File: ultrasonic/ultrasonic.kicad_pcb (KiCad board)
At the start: 2 copper layers, 61 x 36.9 mm, 4 parts, among them J1 Conn_01x23_Female, J2 Conn_01x23_Female, J3 Conn_01x07_Female, J5 Conn_01x04_Male

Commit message: new release
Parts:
- J2: footprint Connector_PinHeader_2.54mm:PinHeader_1x23_P2.54mm_Vertical_SMD_Pin1Left -> Connector_PinSocket_2.54mm:PinSocket_1x23_P2.54mm_Vertical_SMD_Pin1Left

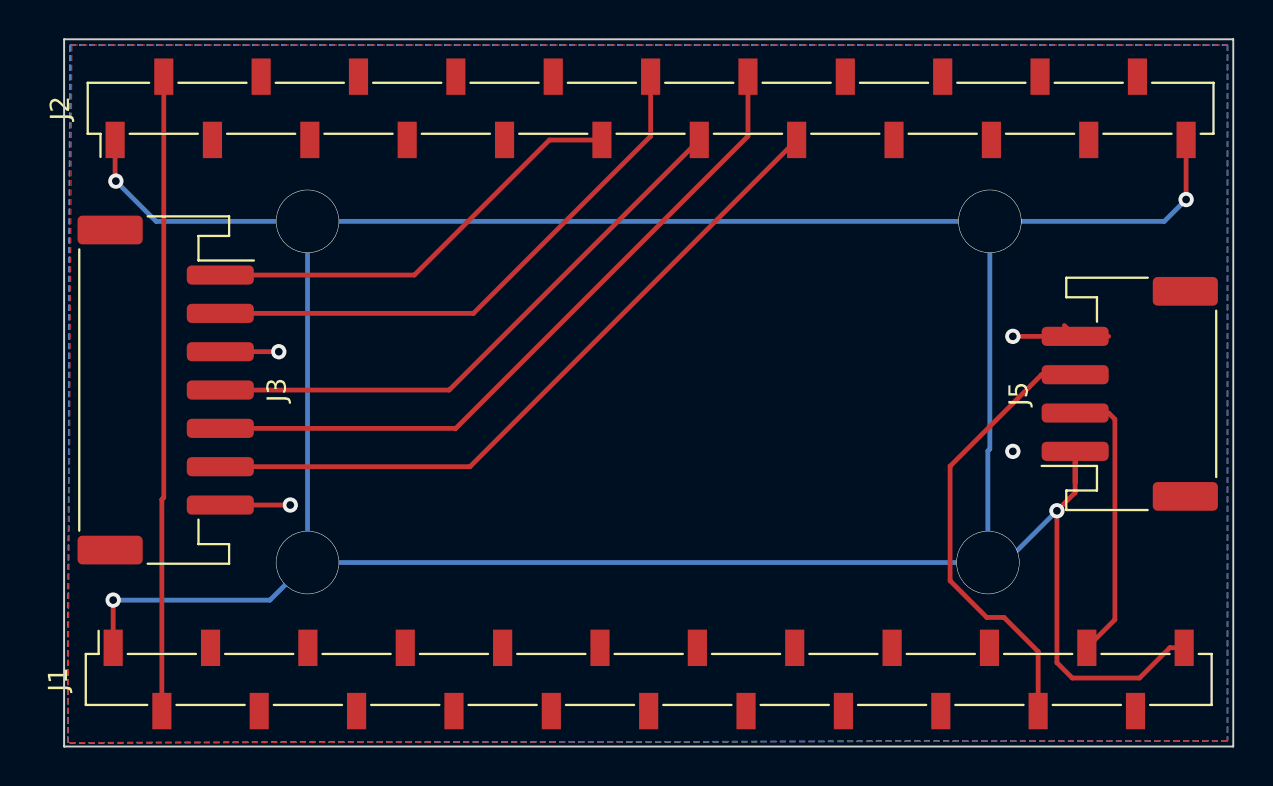
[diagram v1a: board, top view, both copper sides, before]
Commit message: change pinhead to left
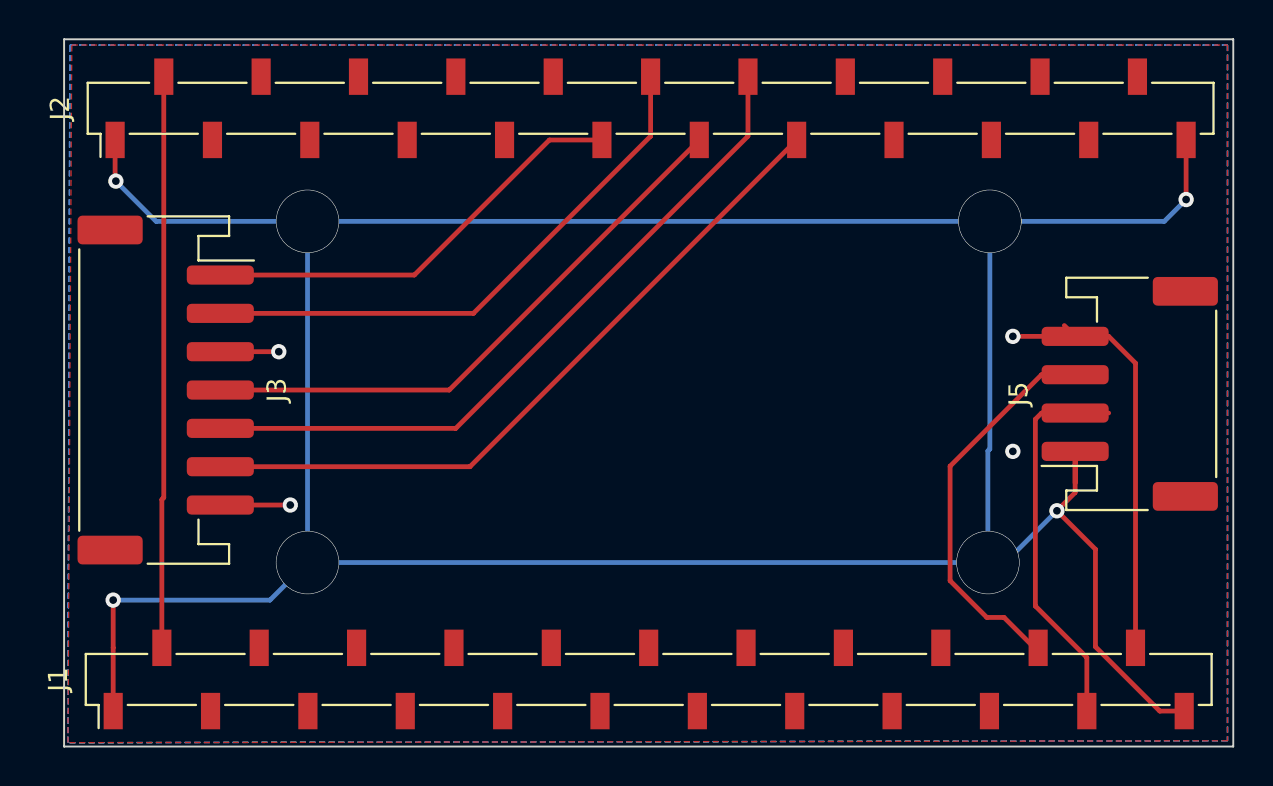
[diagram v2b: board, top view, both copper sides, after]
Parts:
- J1: footprint Connector_PinSocket_2.54mm:PinSocket_1x23_P2.54mm_Vertical_SMD_Pin1Right -> Connector_PinSocket_2.54mm:PinSocket_1x23_P2.54mm_Vertical_SMD_Pin1Left
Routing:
- net +5V: track 10.0 -> 26.8 mm
- net /IO18: track 14.7 -> 20.3 mm
- net +3V3: track 33.4 -> 29.8 mm
- net /IO17: track 23.7 -> 20.6 mm
- net GND: track 175.5 -> 177.2 mm
